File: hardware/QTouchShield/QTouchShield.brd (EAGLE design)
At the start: 100 x 80 mm, 115 parts, among them IC1 AT32UC3C0512CJEDEC-MS-026, U1 ARDUINO-MEGALITE

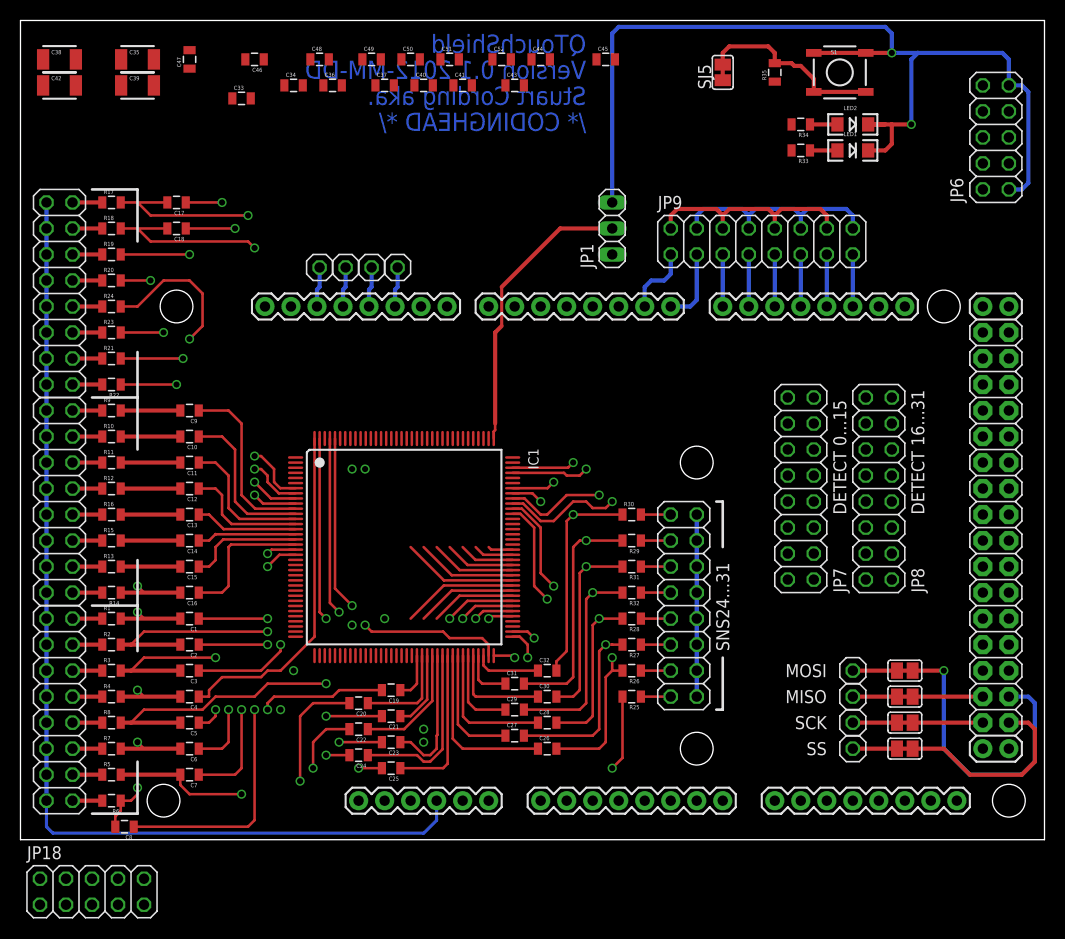
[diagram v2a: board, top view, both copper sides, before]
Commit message: Starting adding decoupling capacitors in correct places.
Decoupling caps being placed near to their associated pins. Not yet
complete.
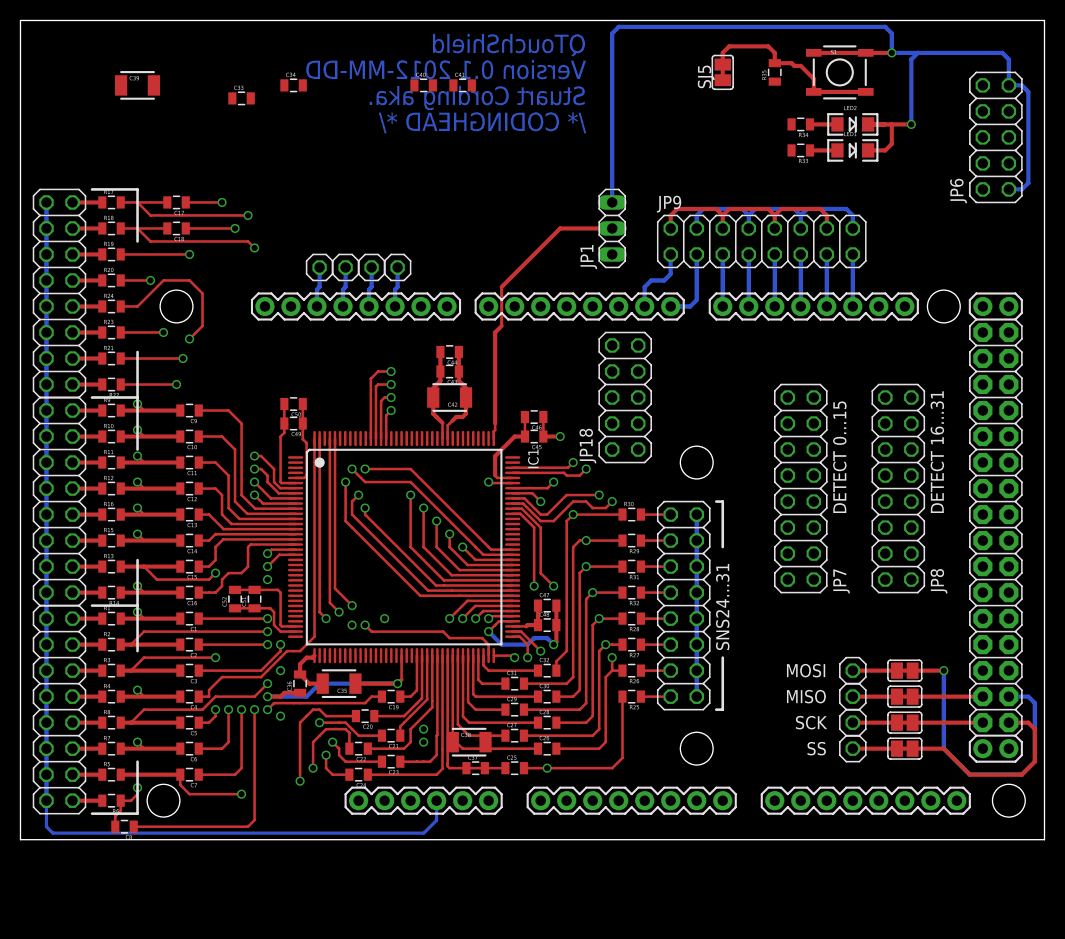
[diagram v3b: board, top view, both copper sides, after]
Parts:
- moved C38 77.8 mm to (43.8, 9.53)
- moved JP18 71.0 mm to (59.1, 43.2), turned to 90 degrees
- moved C37 67.3 mm to (44.5, 6.99)
- moved C35 64.1 mm to (31.1, 15.2), turned to 180 degrees
- moved C47 63.8 mm to (51.4, 22.9), turned to 0 degrees
- moved C48 59.5 mm to (51.4, 21.0)
- moved C52 58.8 mm to (21.0, 23.5), turned to 90 degrees
- moved C36 58.5 mm to (27.3, 15.2), turned to 90 degrees
- moved C51 56.0 mm to (22.9, 23.5), turned to 90 degrees
- moved C42 48.8 mm to (41.9, 43.2), turned to 180 degrees
- moved C46 44.3 mm to (50.2, 41.3)
- moved C45 37.5 mm to (50.2, 39.4), turned to 180 degrees
- moved C49 36.4 mm to (26.7, 40.6), turned to 180 degrees
- moved C50 35.5 mm to (26.7, 42.5), turned to 180 degrees
- moved C44 29.9 mm to (41.9, 47.6), turned to 180 degrees
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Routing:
- net GND: track 218.5 -> 265.6 mm, vias 2 -> 4
- net SNSK8: track 14.2 -> 57.4 mm, vias 0 -> 2
- net SNSK9: track 15.6 -> 55.9 mm, vias 0 -> 2
- net SNSK11: track 17.1 -> 57.0 mm, vias 0 -> 2
- net SNSK12: track 15.7 -> 54.5 mm, vias 0 -> 2
- net SNSK14: track 12.7 -> 50.8 mm, vias 0 -> 3
- net SNSK13: track 14.2 -> 51.9 mm, vias 0 -> 2
- net VCC: track 0.00 -> 37.7 mm, vias 0 -> 2
- net SNSK10: track 17.1 -> 53.0 mm, vias 0 -> 2
- net TOUCH_DATA-MISO: track 0.00 -> 33.3 mm, vias 0 -> 1
- net TOUCH_DATA-MOSI: track 0.00 -> 28.5 mm, vias 0 -> 1
- net VDDIN_33: track 0.00 -> 27.7 mm, vias 0 -> 2
- net TOUCH_DATA-SS: track 0.00 -> 27.6 mm, vias 0 -> 1
- net TOUCH_DATA-SCK: track 0.00 -> 27.4 mm, vias 0 -> 1
- net SNSK16: track 49.8 -> 65.0 mm
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
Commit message: Completed routing of cap sense lines plus JTAG & QT600 Debug IF
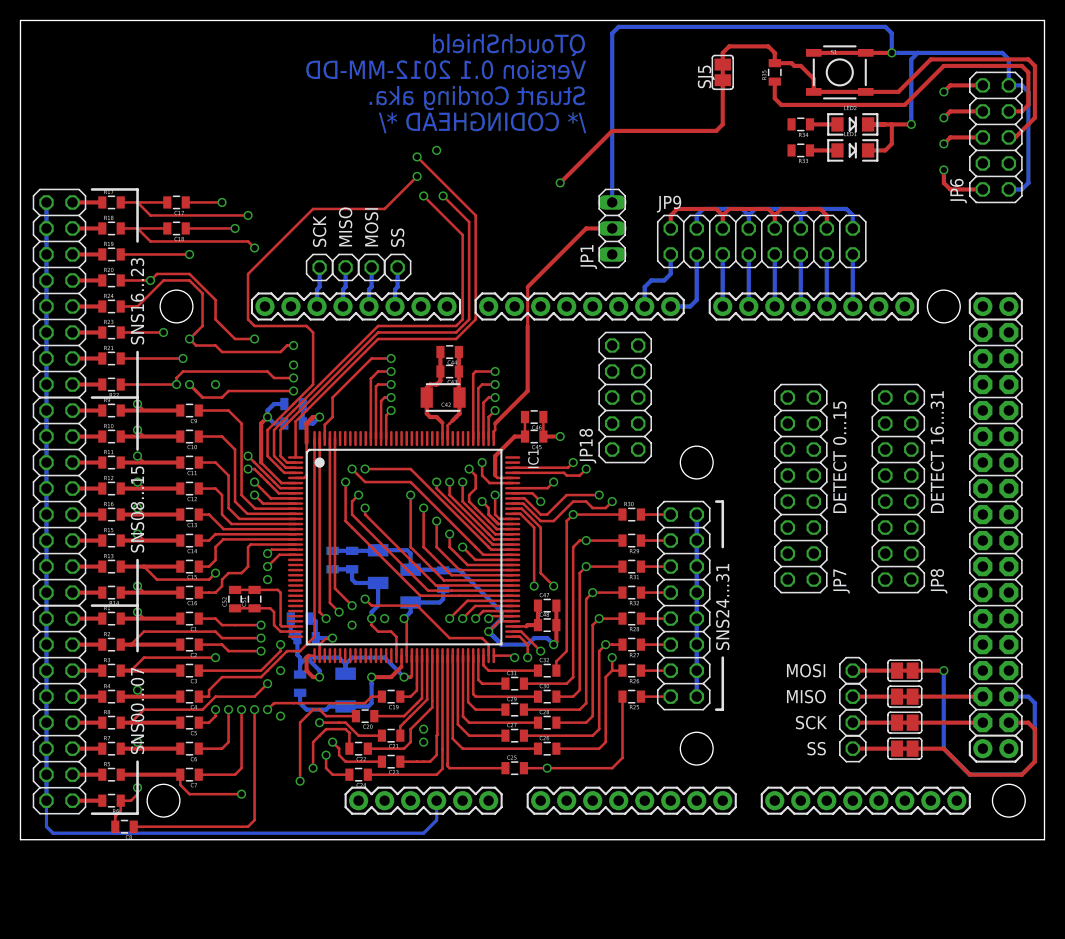
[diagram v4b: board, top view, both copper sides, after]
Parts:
- moved C33 53.1 mm to (27.9, 19.7), flipped to the bottom
- moved C39 52.5 mm to (34.9, 26.7), flipped to the bottom, turned to 90 degrees
- moved C34 52.1 mm to (27.3, 21.6), flipped to the bottom
- moved C41 48.1 mm to (30.5, 27.3), flipped to the bottom, turned to 90 degrees
- moved C40 46.9 mm to (32.4, 27.3), flipped to the bottom, turned to 90 degrees
- moved C37 18.7 mm to (41.3, 25.4), flipped to the bottom, turned to 90 degrees
- moved C38 16.3 mm to (38.1, 24.8), flipped to the bottom, turned to 90 degrees
- moved C35 0.90 mm to (31.8, 14.6), flipped to the bottom, turned to 90 degrees
- moved C42 0.63 mm to (41.3, 43.2)
- flipped C36 to the bottom
- flipped C49 to the bottom, turned to 0 degrees
- flipped C50 to the bottom, turned to 0 degrees
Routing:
- net SDT-SPI0-SCK: track 12.7 -> 124.1 mm, vias 0 -> 1
- net SDT-SPI0-SS: track 25.3 -> 135.2 mm, vias 0 -> 1
- net SDT-SPI0-MISO: track 12.7 -> 122.2 mm, vias 0 -> 1
- net JTAG_TCK: track 0.00 -> 106.9 mm, vias 0 -> 2
- net JTAG_TMS: track 0.00 -> 105.9 mm, vias 0 -> 2
- net JTAG_TDO: track 0.00 -> 102.1 mm, vias 0 -> 3
- net SDT-SPI0-MOSI: track 35.5 -> 135.2 mm, vias 1 -> 2
- net JTAG_TDI: track 0.00 -> 95.6 mm, vias 0 -> 2
- net JTAG_RESET: track 20.3 -> 109.4 mm, vias 0 -> 2
- net VCC: track 37.7 -> 97.9 mm, vias 2 -> 5
- net GND: track 265.6 -> 318.3 mm, vias 4 -> 7
- net SNSK21: track 68.9 -> 118.3 mm, vias 2 -> 3
- net SNSK19: track 76.9 -> 125.5 mm, vias 2 -> 5
- net SNSK22: track 64.8 -> 107.8 mm, vias 2 -> 5
- net SNSK20: track 72.4 -> 114.4 mm, vias 2 -> 4
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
